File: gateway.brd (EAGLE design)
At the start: 100 x 100 mm, 14 parts, among them J1 RASPBERRYPI-40-PIN-GPIO_PTH_N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, Q1 BSS123

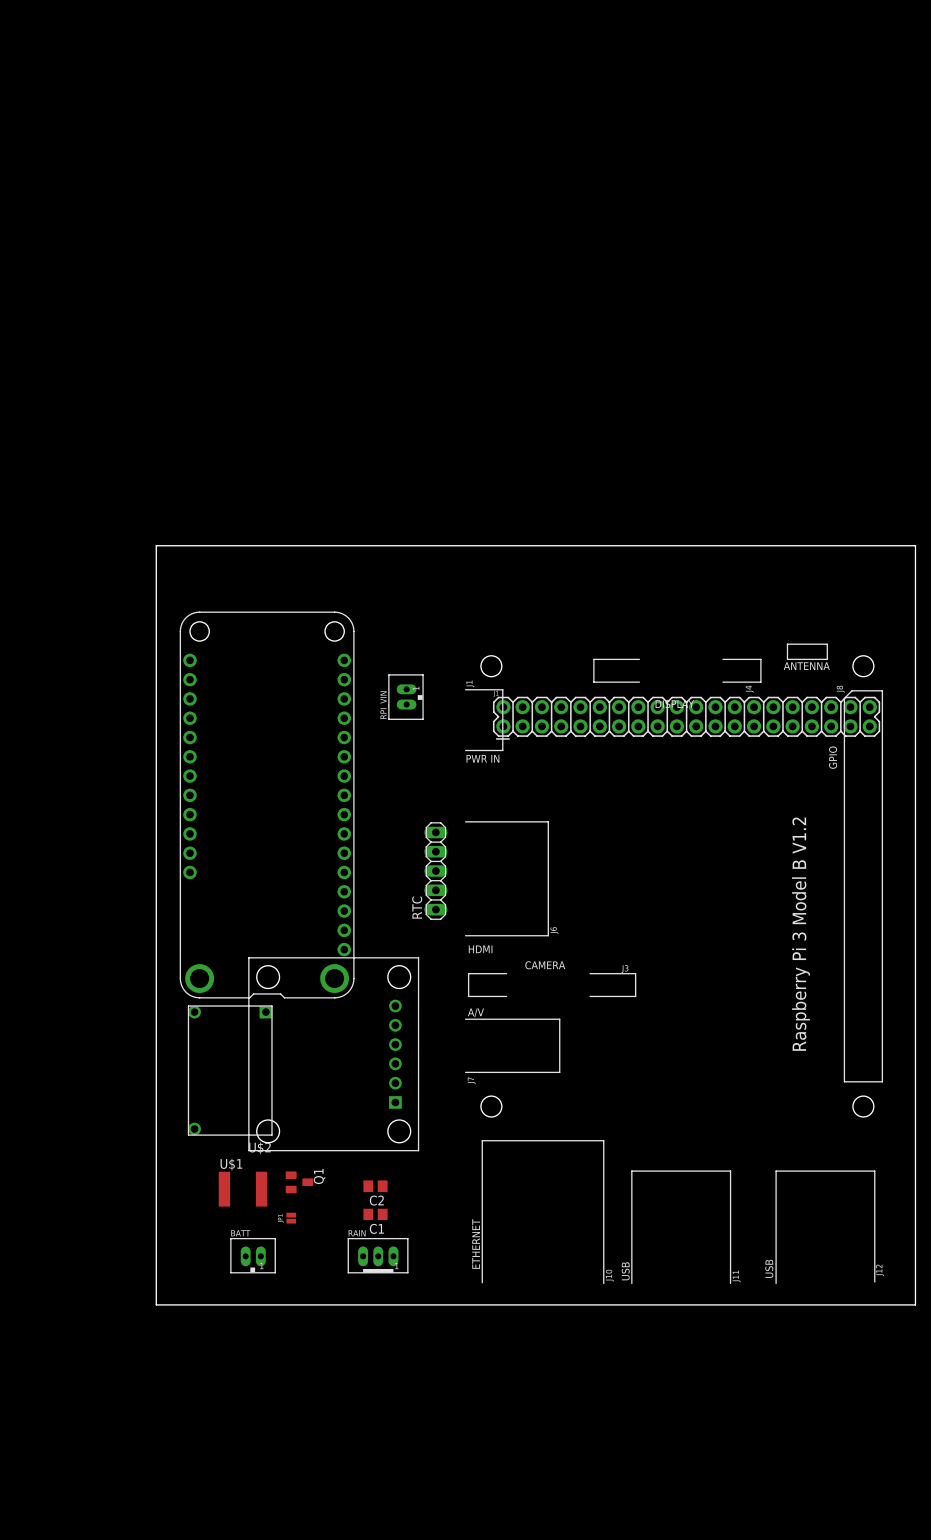
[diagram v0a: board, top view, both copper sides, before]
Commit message: added solar charge controller and delay timer. still need edits on the supply line of feather board.
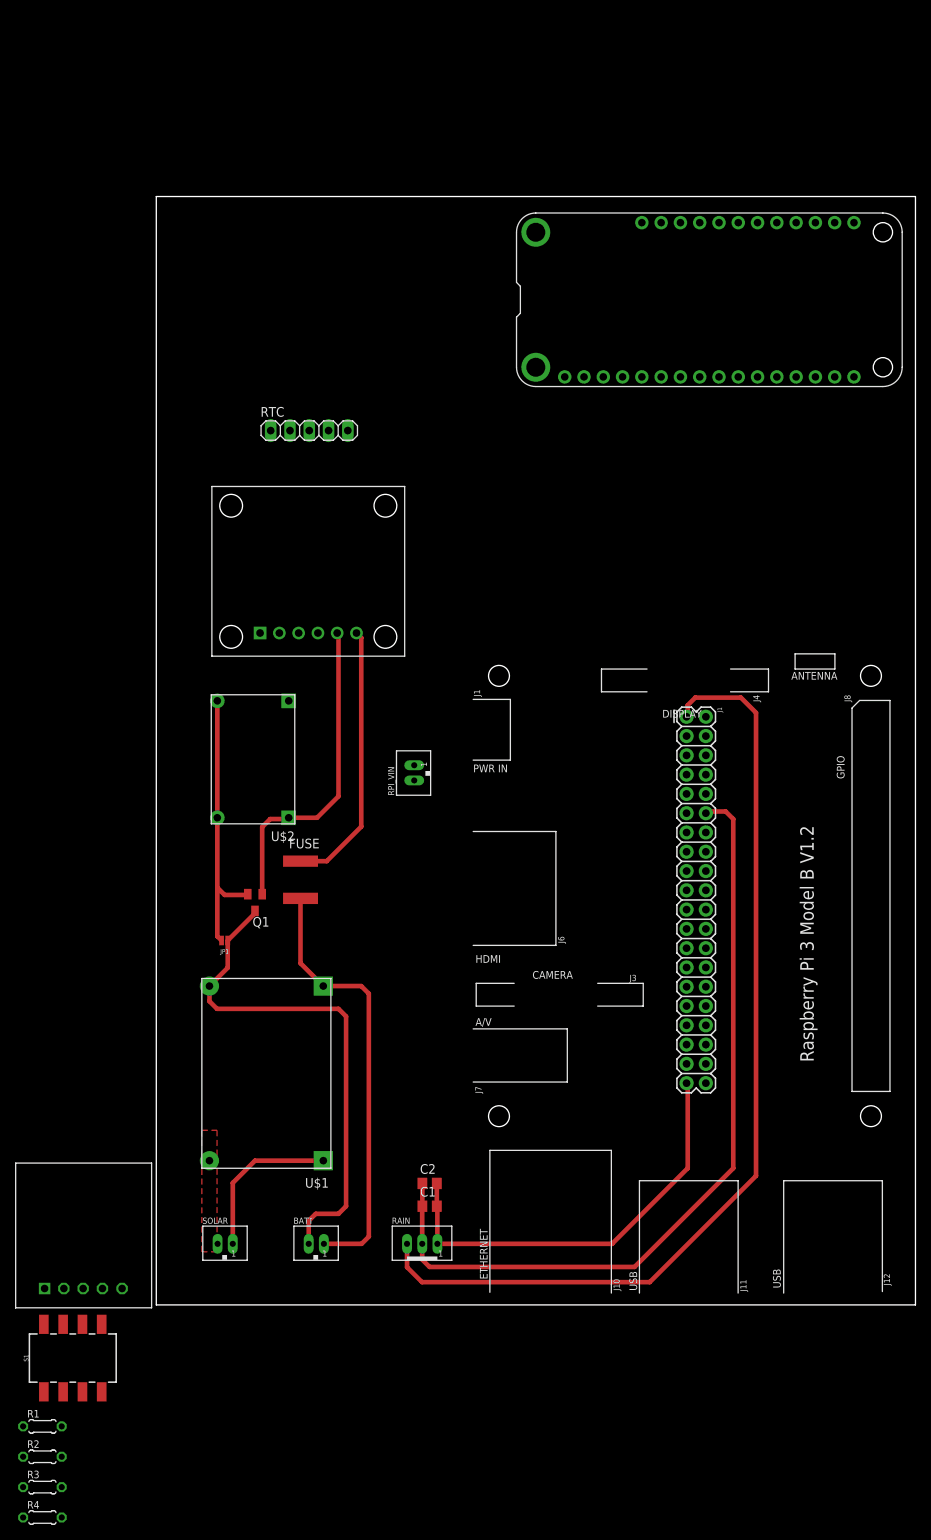
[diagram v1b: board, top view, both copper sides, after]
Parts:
- added FUSE: MF-SMDF200, fuse:MF-SMDF050
- added R1, R2, R3, R4: (no value), rcl:0204/5
- added S1: DIP-04SMD, SparkFun-Switches:DIPSWITCH-04-SMD
- added SOLAR: JST-PH_2-PIN_HEADER, SRG:JST_B2B-PH_HEADER
- added U$3: TPL5110_BREAKOUT, edc_modules:TPL5110_BREAKOUT
- U$1: value MF-SMDF200 -> TP5100; device fuse:MF-SMDF050 -> edc_modules:TP5100
- moved MS1 83.3 mm to (47.5, 121.0), turned to 0 degrees
- moved RTC 60.4 mm to (20.1, 115.2), turned to 0 degrees
- moved INA219 54.4 mm to (20.0, 85.5), turned to 0 degrees
- moved U$2 41.1 mm to (18.2, 80.4)
- moved JP1 37.6 mm to (9.00, 48.0), turned to 180 degrees
- moved Q1 37.3 mm to (13.0, 53.0), turned to 180 degrees
- moved U$1 30.1 mm to (23.0, 43.0), turned to 180 degrees
- moved J1 24.2 mm to (69.8, 77.5), turned to 270 degrees
- moved RPI_VIN 10.0 mm to (34.0, 70.0)
- moved BATT 8.46 mm to (21.0, 8.00)
- moved C1 7.22 mm to (36.0, 13.0), turned to 0 degrees
- moved C2 7.15 mm to (36.0, 16.0), turned to 0 degrees
- moved RAIN 6.02 mm to (35.0, 8.00)
- moved PCB2 1.62 mm to (41.6, 86.4)
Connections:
- removed net N$2: BATT.P2, U$1.1
- new net BATT+: BATT.P1, FUSE.1, U$1.VOUT+
- new net BATT-: BATT.P2, JP1.1, Q1.3, U$1.VOUT-
- new net DELAY: S1.5, S1.6, S1.7, S1.8, U$3.DELAY
- new net N$10: R2.2, S1.3
- new net N$11: R3.2, S1.2
- new net N$12: R4.2, S1.1
- new net N$8: SOLAR.P1, U$1.VIN+
- new net N$9: R1.2, S1.4
- new net RPI_GPIO22: J1.15, U$3.DONE
- new net SOLAR-: SOLAR.P2, U$1.VIN-
- net +5V: now also U$3.VDD
- net GND: now also R1.1, R2.1, R3.1, R4.1, U$3.GND
- net N$6: now also FUSE.2; no longer U$1.2
- net N$7: now also U$3.DRV; no longer BATT.P1, JP1.1, Q1.3
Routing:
- net +3V3: track 0.00 -> 128.5 mm
- net RPI_GPIO18: track 0.00 -> 106.9 mm
- net GND: track 0.00 -> 92.6 mm
- net BATT-: track 0.00 -> 67.0 mm
- net BATT+: track 0.00 -> 57.5 mm
- net N$5: track 0.00 -> 42.2 mm
- net N$6: track 0.00 -> 35.6 mm
- net N$8: track 0.00 -> 21.2 mm
- added copper zone on layer 1, net N$2
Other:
- board size 100 x 100 mm -> 100 x 146 mm

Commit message: added another rtc for feather ( tilt only config )
added the bno05_breakout footprint
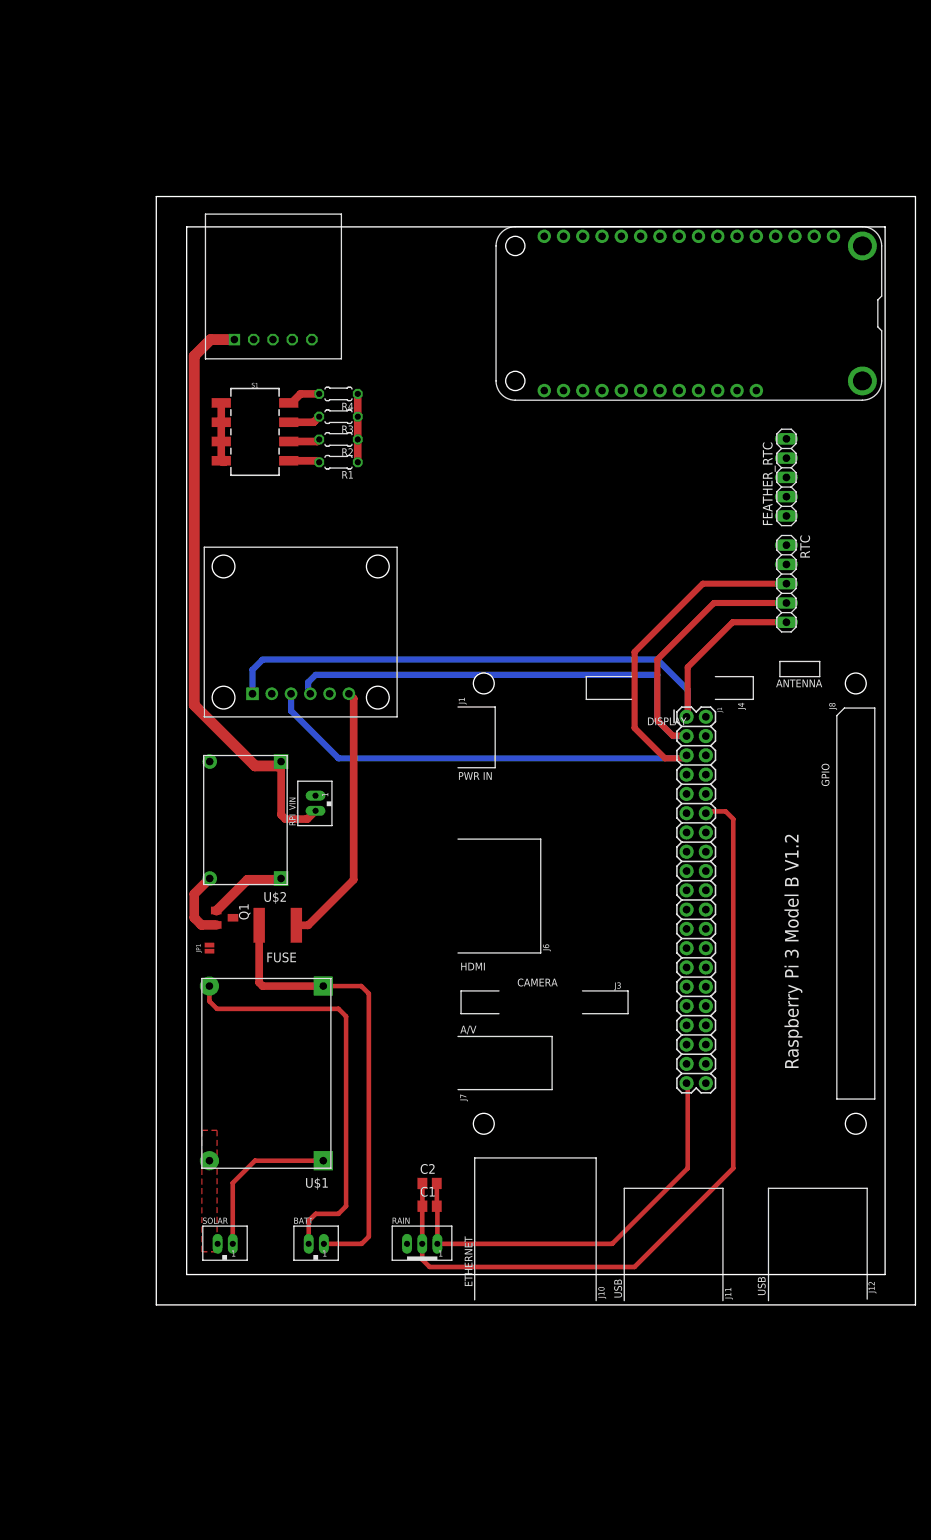
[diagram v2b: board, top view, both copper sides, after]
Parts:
- added FEATHER_RTC: (no value), pinhead:1X05
- moved R4 153.1 mm to (24.0, 120.0), turned to 180 degrees
- moved R3 146.3 mm to (24.0, 117.0), turned to 180 degrees
- moved R2 139.6 mm to (24.0, 114.0), turned to 180 degrees
- moved R1 132.9 mm to (24.0, 111.0), turned to 180 degrees
- moved U$3 127.5 mm to (8.00, 125.0)
- moved S1 124.3 mm to (13.0, 115.0), turned to 270 degrees
- moved RTC 66.0 mm to (83.0, 95.0), turned to 270 degrees
- moved MS1 52.5 mm to (95.5, 142.0), turned to 180 degrees
- moved RPI_VIN 13.6 mm to (21.0, 66.0)
- moved INA219 8.06 mm to (19.0, 77.5)
- moved U$2 8.06 mm to (17.2, 72.4)
- moved FUSE 6.71 mm to (16.0, 50.0), turned to 0 degrees
- moved Q1 4.47 mm to (9.00, 51.0), turned to 270 degrees
- moved JP1 2.24 mm to (7.00, 47.0), turned to 90 degrees
- moved PCB2 2.24 mm to (39.6, 85.4)
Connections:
- removed net N$1: RTC.5
- removed net RPI_GPIO22: J1.15, U$3.DONE
- new net DONE_PIN: MS1.5, U$3.DONE
- new net FEATHER_3.3V: FEATHER_RTC.5, MS1.2
- new net FEATHER_SCL: FEATHER_RTC.3, MS1.18
- new net FEATHER_SDA: FEATHER_RTC.4, MS1.17
- net +3V3: now also RTC.5
- net GND: now also FEATHER_RTC.1
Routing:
- net RPI_SCL: track 0.00 -> 99.5 mm
- net RPI_SDA: track 0.00 -> 91.5 mm
- net +5V: track 0.00 -> 79.4 mm
- net +3V3: track 128.5 -> 88.3 mm
- net N$5: track 42.2 -> 10.3 mm
- net GND: track 92.6 -> 74.7 mm
- net BATT-: track 67.0 -> 54.6 mm
- net DELAY: track 0.00 -> 8.52 mm
- net N$12: track 0.00 -> 4.51 mm
- net N$11: track 0.00 -> 4.32 mm
- net N$10: track 0.00 -> 4.13 mm
- net N$9: track 0.00 -> 4.09 mm
- net BATT+: track 57.5 -> 60.9 mm
- net N$6: track 35.6 -> 34.8 mm
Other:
- outline, holes or cut-outs redrawn

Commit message: finished routing
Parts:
- added TILT_SUPPLY: (no value), SparkFun-Jumpers:SMT-JUMPER_2_NO_NO-SILK
- added U$4: BNO05_BREAKOUT, edc_modules:BNO05_BREAKOUT
- INA219: value INA219 -> (none)
- moved RPI_VIN 18.4 mm to (7.98, 79.0), turned to 270 degrees
- moved INA219 7.07 mm to (18.0, 84.5)
- moved FUSE 6.00 mm to (22.0, 50.0), turned to 90 degrees
- moved Q1 2.50 mm to (11.5, 51.0), turned to 180 degrees
- moved MS1 1.41 mm to (94.5, 141.0)
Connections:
- net N$5 renamed INA_VIN-
- net N$6 renamed INA_VIN+
- net N$8 renamed SOLAR+
- removed net 5V: J1.2, J1.4
- removed net N$7: U$3.DRV
- removed net USB: MS1.26
- new net FEATHER_USB: MS1.26, TILT_SUPPLY.2, U$3.DRV
- new net N$1: MS1.27
- new net N$2: J1.2
- new net N$3: J1.4
- new net VIN: U$4.VIN
- net +3V3: no longer INA219.P$1, RAIN.P3
- net +5V: now also TILT_SUPPLY.1
- net FEATHER_3.3V: now also INA219.P$1, RAIN.P3, U$4.3V3
- net FEATHER_SCL: now also U$4.SCL
- net FEATHER_SDA: now also U$4.SDA
- net GND: now also U$4.GND
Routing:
- net FEATHER_3.3V: track 0.00 -> 278.7 mm
- net RPI_TX: track 0.00 -> 128.4 mm
- net RPI_RX: track 0.00 -> 122.6 mm
- net FEATHER_SCL: track 0.00 -> 94.0 mm
- net FEATHER_SDA: track 0.00 -> 81.8 mm
- net GND: track 74.7 -> 144.2 mm
- net DONE_PIN: track 0.00 -> 68.2 mm
- net +3V3: track 88.3 -> 22.0 mm
- net FEATHER_USB: track 0.00 -> 65.5 mm
- net INA_VIN+: track 34.8 -> 6.56 mm
- net +5V: track 79.4 -> 53.0 mm
- net BATT+: track 60.9 -> 44.7 mm
- net DELAY: track 8.52 -> 22.0 mm
- net RPI_SCL: track 99.5 -> 103.4 mm
- net INA_VIN-: track 10.3 -> 7.26 mm
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- added copper zone on layer 1, net +5V
- added copper zone on layer 1, net BATT+
- added copper zone on layer 1, net BATT-
- added copper zone on layer 1, net FEATHER_USB
- added copper zone on layer 1, net GND
- added copper zone on layer 16, net GND
- added copper zone on layer 1, net INA_VIN+
- added copper zone on layer 1, net INA_VIN-
- added copper zone on layer 1, net SOLAR+
- added copper zone on layer 1, net SOLAR-
- removed copper zone on layer 1, net N$2
